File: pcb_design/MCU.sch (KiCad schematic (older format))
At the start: 14 parts, among them U1 STM32F40X_LQFP64, X2 ABM3B - 8MHz

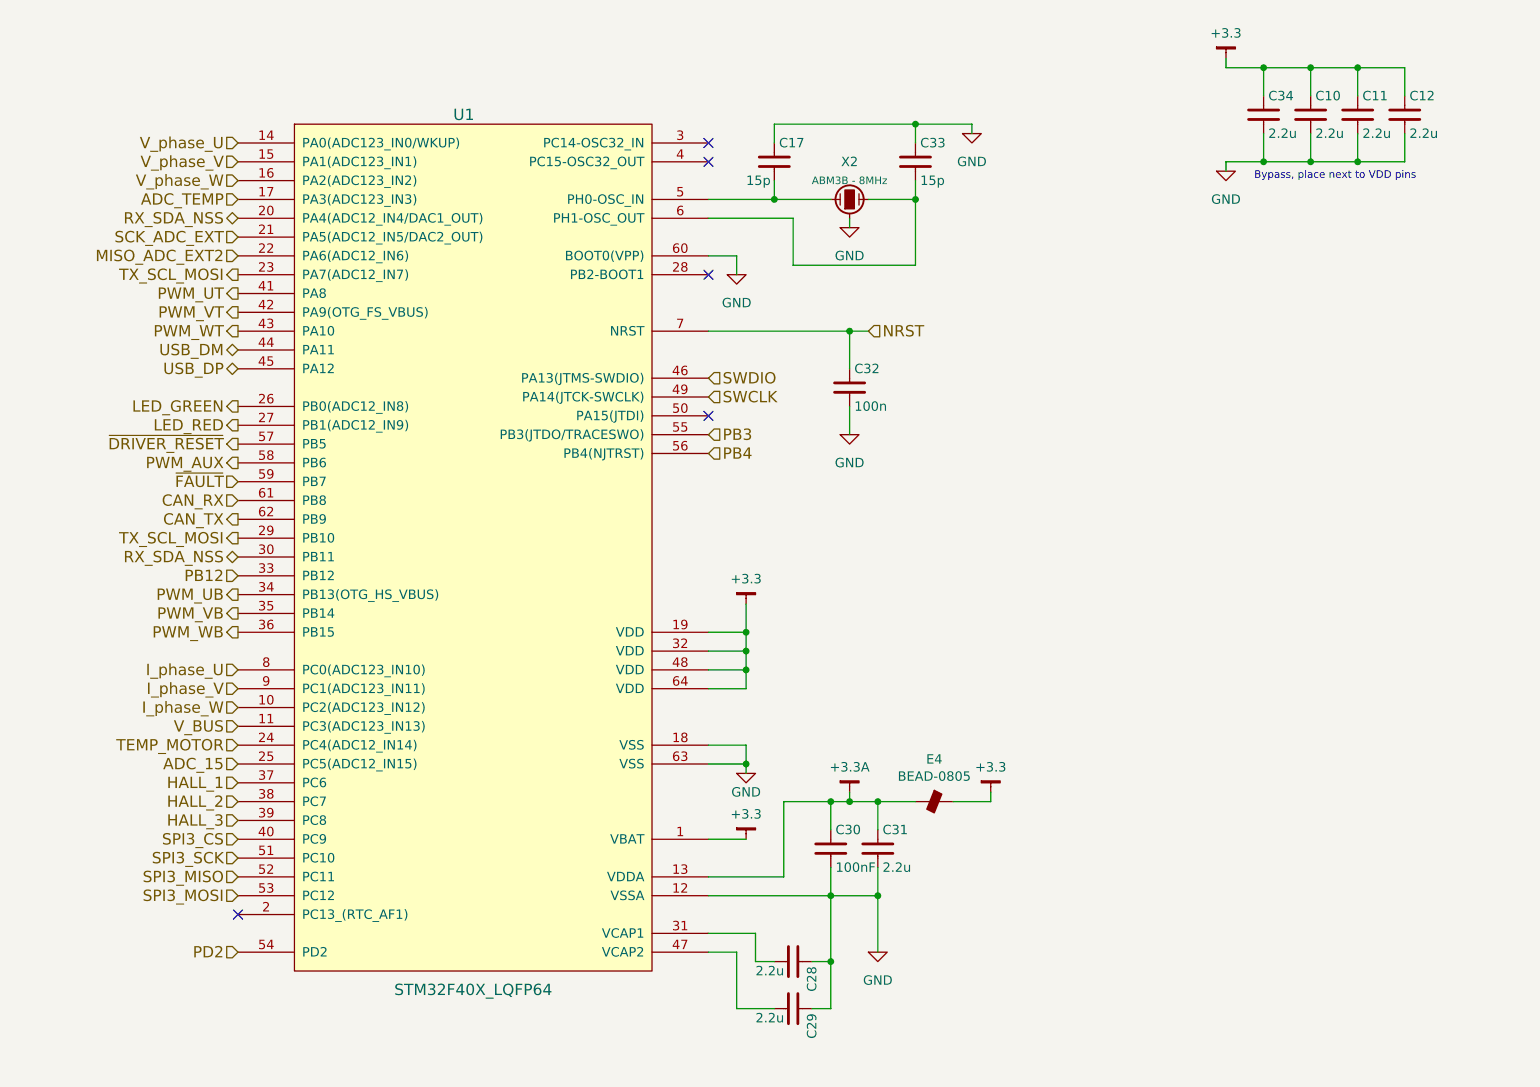
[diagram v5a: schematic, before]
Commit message: Fixed issue with non-bidirectional phase current measurement. Started routing power supplies. Changed terminal blocks from 5.00mm to 3.81mm pitch
Signed-off-by: Marcos Chaparro <mchaparro@paltatech.com>
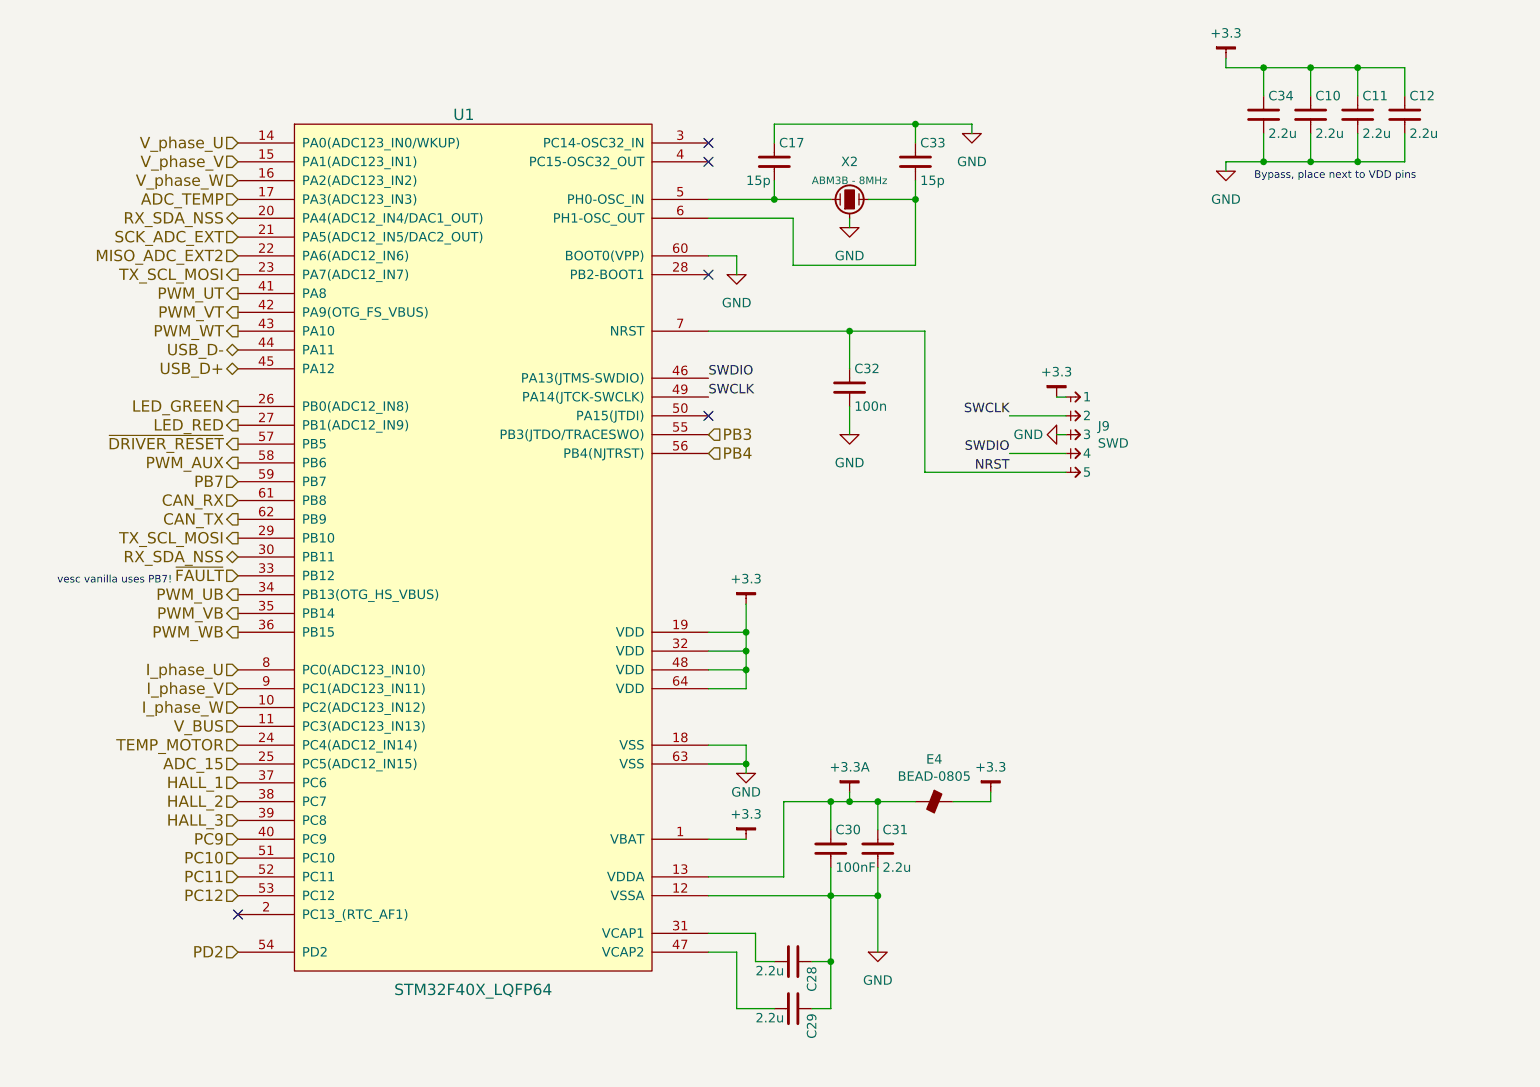
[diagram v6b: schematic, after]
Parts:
- added J9: SWD, conn-100mil:CONN-100MIL-M-1x5, symbol CONN-100MIL-M-1x5
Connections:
- net PB12 is gone; now on net ~FAULT: U1.33 (PB12)
- net +3.3: now also J9.1
- net GND: now also J9.3
- net NRST: now also J9.5
- net SWCLK: now also J9.2
- net SWDIO: now also J9.4
- net ~FAULT: no longer U1.59 (PB7)
- net SPI3_CS renamed PC9
- net SPI3_MISO renamed PC11
- net SPI3_MOSI renamed PC12
- net SPI3_SCK renamed PC10
- net USB_DM renamed USB_D-
- net USB_DP renamed USB_D+
- new net PB7: U1.59 (PB7)
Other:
- note added: "vesc vanilla uses PB7!"
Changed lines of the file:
@@
 Sheet 12 13
 Title "VESC 6.4"
-Date "2016-07-07"
-Rev "A"
-Comp "Benjamin Vedder"
+Date "2017-01-24"
+Rev "0.1"
+Comp "vedder.se + PALTA TECH S.A. + PYMCO.fr"
 Comment1 ""
 Comment2 ""
@@
 $EndDescr
 Text HLabel 3650 2600 0    60   BiDi ~ 0
-USB_DM
+USB_D-
 Text HLabel 3650 2700 0    60   BiDi ~ 0
-USB_DP
+USB_D+
 Text HLabel 3650 3200 0    60   Output ~ 0
 PWM_AUX
@@
 Text HLabel 3650 2000 0    60   Input ~ 0
 SCK_ADC_EXT
-Text HLabel 3650 3300 0    60   Input ~ 0
+Text HLabel 3650 3800 0    60   Input ~ 0
 ~FAULT
 Text HLabel 3650 2500 0    60   Output ~ 0
@@
 	8900 1650 8900 1600
 Wire Wire Line
-	6150 2500 7000 2500
+	6150 2500 7300 2500
 Wire Wire Line
 	6900 2500 6900 2700
@@
 Bypass, place next to VDD pins
 $Comp
-L GND #PWR150
+L GND #PWR0145
 U 1 1 572D84DC
 P 7550 1450
-F 0 "#PWR150" H 7550 1200 50  0001 C CNN
+F 0 "#PWR0145" H 7550 1200 50  0001 C CNN
 F 1 "GND" H 7550 1300 50  0000 C CNN
 F 2 "" H 7550 1450 60  0000 C CNN
@@
 $EndComp
 $Comp
-L GND #PWR146
+L GND #PWR0146
 U 1 1 572D84DF
 P 6900 1950
-F 0 "#PWR146" H 6900 1700 50  0001 C CNN
+F 0 "#PWR0146" H 6900 1700 50  0001 C CNN
 F 1 "GND" H 6900 1800 50  0000 C CNN
 F 2 "" H 6900 1950 60  0000 C CNN
@@
 $EndComp
 $Comp
-L GND #PWR142
+L GND #PWR0147
 U 1 1 572D84E0
 P 6300 2200
-F 0 "#PWR142" H 6300 1950 50  0001 C CNN
+F 0 "#PWR0147" H 6300 1950 50  0001 C CNN
 F 1 "GND" H 6300 2050 50  0000 C CNN
 F 2 "" H 6300 2200 60  0000 C CNN
@@
 $EndComp
 $Comp
-L GND #PWR147
+L GND #PWR0148
 U 1 1 572D84E2
 P 6900 3050
-F 0 "#PWR147" H 6900 2800 50  0001 C CNN
+F 0 "#PWR0148" H 6900 2800 50  0001 C CNN
 F 1 "GND" H 6900 2900 50  0000 C CNN
 F 2 "" H 6900 3050 60  0000 C CNN
@@
 Wire Wire Line
 	6900 3050 6900 2900
-Text HLabel 7000 2500 2    60   Input ~ 0
-NRST
-Text HLabel 6150 2750 2    60   Input ~ 0
-SWDIO
-Text HLabel 6150 2850 2    60   Input ~ 0
-SWCLK
-$Comp
-L GND #PWR149
+$Comp
+L GND #PWR0149
 U 1 1 572D84E3
 P 7050 5800
-F 0 "#PWR149" H 7050 5550 50  0001 C CNN
+F 0 "#PWR0149" H 7050 5550 50  0001 C CNN
 F 1 "GND" H 7050 5650 50  0000 C CNN
 F 2 "" H 7050 5800 60  0000 C CNN
@@
 $EndComp
 $Comp
-L GND #PWR144
+L GND #PWR0150
 U 1 1 572D84E4
 P 6350 4850
-F 0 "#PWR144" H 6350 4600 50  0001 C CNN
+F 0 "#PWR0150" H 6350 4600 50  0001 C CNN
 F 1 "GND" H 6350 4750 50  0000 C CNN
 F 2 "" H 6350 4850 60  0000 C CNN
@@
 $EndComp
 $Comp
-L GND #PWR153
+L GND #PWR0151
 U 1 1 572D84E9
 P 8900 1650
-F 0 "#PWR153" H 8900 1400 50  0001 C CNN
+F 0 "#PWR0151" H 8900 1400 50  0001 C CNN
 F 1 "GND" H 8900 1500 50  0000 C CNN
 F 2 "" H 8900 1650 60  0000 C CNN
@@
 I_phase_W
 Text HLabel 3650 5400 0    60   Input ~ 0
-SPI3_MISO
+PC11
 Text HLabel 3650 5500 0    60   Input ~ 0
-SPI3_MOSI
+PC12
 Text HLabel 3650 5300 0    60   Input ~ 0
-SPI3_SCK
+PC10
 Text HLabel 3650 5200 0    60   Input ~ 0
-SPI3_CS
+PC9
 NoConn ~ 3650 5600
 Text HLabel 3650 4800 0    60   Input ~ 0
 ADC_15
-Text HLabel 3650 3800 0    60   Input ~ 0
-PB12
+Text HLabel 3650 3300 0    60   Input ~ 0
+PB7
 Text HLabel 3650 5800 0    60   Input ~ 0
 PD2
@@
 $EndComp
 $Comp
-L +3.3 #PWR152
+L +3.3 #PWR0152
 U 1 1 588B6A3F
 P 8900 1050
-F 0 "#PWR152" H 0   100 30  0001 C CNN
+F 0 "#PWR0152" H 0   100 30  0001 C CNN
 F 1 "+3.3" H 8900 1183 50  0000 C CNN
 F 2 "" H 0   50  60  0000 C CNN
@@
 Connection ~ 6900 2500
 $Comp
-L +3.3 #PWR143
+L +3.3 #PWR0153
 U 1 1 588B6C25
 P 6350 3950
-F 0 "#PWR143" H 6400 4000 30  0001 C CNN
+F 0 "#PWR0153" H 6400 4000 30  0001 C CNN
 F 1 "+3.3" H 6350 4083 50  0000 C CNN
 F 2 "" H 0   50  60  0000 C CNN
@@
 $EndComp
 $Comp
-L +3.3 #PWR151
+L +3.3 #PWR0154
 U 1 1 588B6CC6
 P 7650 4950
-F 0 "#PWR151" H 7700 5000 30  0001 C CNN
+F 0 "#PWR0154" H 7700 5000 30  0001 C CNN
 F 1 "+3.3" H 7650 5083 50  0000 C CNN
 F 2 "" H 0   50  60  0000 C CNN
@@
 $EndComp
 $Comp
-L +3.3 #PWR145
+L +3.3 #PWR0155
 U 1 1 588B6D3A
 P 6350 5200
-F 0 "#PWR145" H 6400 5250 30  0001 C CNN
+F 0 "#PWR0155" H 6400 5250 30  0001 C CNN
 F 1 "+3.3" H 6350 5333 50  0000 C CNN
 F 2 "" H -1300 300 60  0000 C CNN
@@
 $EndComp
 $Comp
-L +3.3A #PWR148
+L +3.3A #PWR0156
 U 1 1 588B9943
 P 6900 4950
-F 0 "#PWR148" H 6950 5000 30  0001 C CNN
+F 0 "#PWR0156" H 6950 5000 30  0001 C CNN
 F 1 "+3.3A" H 6900 5083 50  0000 C CNN
 F 2 "" H -900 -500 60  0000 C CNN
@@
 	6900 4950 6900 5000
 Connection ~ 6900 5000
+$Comp
+L CONN-100MIL-M-1x5 J9
+U 1 1 5892AE40
+P 8100 2850
+F 0 "J9" H 8219 2695 50  0000 L CNN
+F 1 "SWD" H 8219 2604 50  0000 L CNN
+F 2 "conn-100mil:CONN-100MIL-M-1x5" H -450 -550 50  0001 C CNN
+F 3 "" H -450 -550 50  0000 C CNN
+	1    8100 2850
+	1    0    0    -1
+$EndComp
+$Comp
+L +3.3 #PWR0157
+U 1 1 5892B530
+P 8000 2850
+F 0 "#PWR0157" H -900 1900 30  0001 C CNN
+F 1 "+3.3" H 8000 2983 50  0000 C CNN
+F 2 "" H -900 1850 60  0000 C CNN
+F 3 "" H -900 1850 60  0000 C CNN
+	1    8000 2850
+	1    0    0    -1
+$EndComp
+Wire Wire Line
+	8000 2850 8050 2850
+Text Label 6150 2850 0    50   ~ 0
+SWCLK
+Text Label 6150 2750 0    50   ~ 0
+SWDIO
+Text Label 7750 3150 2    50   ~ 0
+SWDIO
+Wire Wire Line
+	7750 3150 8050 3150
+Wire Wire Line
+	8050 2950 7750 2950
+$Comp
+L GND #PWR0158
+U 1 1 5892B905
+P 8000 3050
+F 0 "#PWR0158" H 8000 2800 50  0001 C CNN
+F 1 "GND" V 8000 2900 50  0000 C CNN
+F 2 "" H 8000 3050 60  0000 C CNN
+F 3 "" H 8000 3050 60  0000 C CNN
+	1    8000 3050
+	0    1    1    0
+$EndComp
+Wire Wire Line
+	8000 3050 8050 3050
+Text Label 7750 2950 2    50   ~ 0
+SWCLK
+Wire Wire Line
+	8050 3250 7300 3250
+Wire Wire Line
+	7300 3250 7300 2500
+Text Label 7750 3250 2    50   ~ 0
+NRST
+Text Notes 3300 3850 2    40   ~ 0
+vesc vanilla uses PB7!
 $EndSCHEMATC

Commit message: More layout
Signed-off-by: Marcos Chaparro <mchaparro@paltatech.com>
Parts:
- added R122: 1k, IPC7351-Nominal:RESC1608X50, symbol R-0603
- added SW1: BOOTLOADER, symbol PUSH
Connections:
- net +3.3: now also SW1.2
- net GND: now also R122.2; no longer U1.60 (BOOT0(VPP))
- new net: R122.1, SW1.1, U1.60 (BOOT0(VPP))
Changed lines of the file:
@@
 	6350 3950 6350 4400
 Wire Wire Line
-	6300 2100 6300 2200
-Wire Wire Line
-	6150 2100 6300 2100
+	6450 2350 6450 2400
 Connection ~ 7250 1400
 Wire Wire Line
@@
 Bypass, place next to VDD pins
 $Comp
-L GND #PWR0145
+L GND #PWR154
 U 1 1 572D84DC
 P 7550 1450
-F 0 "#PWR0145" H 7550 1200 50  0001 C CNN
+F 0 "#PWR154" H 7550 1200 50  0001 C CNN
 F 1 "GND" H 7550 1300 50  0000 C CNN
 F 2 "" H 7550 1450 60  0000 C CNN
@@
 $EndComp
 $Comp
-L GND #PWR0146
+L GND #PWR149
 U 1 1 572D84DF
 P 6900 1950
-F 0 "#PWR0146" H 6900 1700 50  0001 C CNN
+F 0 "#PWR149" H 6900 1700 50  0001 C CNN
 F 1 "GND" H 6900 1800 50  0000 C CNN
 F 2 "" H 6900 1950 60  0000 C CNN
@@
 $EndComp
 $Comp
-L GND #PWR0147
+L GND #PWR148
 U 1 1 572D84E0
-P 6300 2200
-F 0 "#PWR0147" H 6300 1950 50  0001 C CNN
-F 1 "GND" H 6300 2050 50  0000 C CNN
-F 2 "" H 6300 2200 60  0000 C CNN
-F 3 "" H 6300 2200 60  0000 C CNN
-	1    6300 2200
+P 6450 2400
+F 0 "#PWR148" H 6450 2150 50  0001 C CNN
+F 1 "GND" H 6450 2300 50  0000 C CNN
+F 2 "" H 6450 2400 60  0000 C CNN
+F 3 "" H 6450 2400 60  0000 C CNN
+	1    6450 2400
 	1    0    0    -1
 $EndComp
@@
 $EndComp
 $Comp
-L GND #PWR0148
+L GND #PWR150
 U 1 1 572D84E2
 P 6900 3050
-F 0 "#PWR0148" H 6900 2800 50  0001 C CNN
+F 0 "#PWR150" H 6900 2800 50  0001 C CNN
 F 1 "GND" H 6900 2900 50  0000 C CNN
 F 2 "" H 6900 3050 60  0000 C CNN
@@
 	6900 3050 6900 2900
 $Comp
-L GND #PWR0149
+L GND #PWR152
 U 1 1 572D84E3
 P 7050 5800
-F 0 "#PWR0149" H 7050 5550 50  0001 C CNN
+F 0 "#PWR152" H 7050 5550 50  0001 C CNN
 F 1 "GND" H 7050 5650 50  0000 C CNN
 F 2 "" H 7050 5800 60  0000 C CNN
@@
 $EndComp
 $Comp
-L GND #PWR0150
+L GND #PWR146
 U 1 1 572D84E4
 P 6350 4850
-F 0 "#PWR0150" H 6350 4600 50  0001 C CNN
+F 0 "#PWR146" H 6350 4600 50  0001 C CNN
 F 1 "GND" H 6350 4750 50  0000 C CNN
 F 2 "" H 6350 4850 60  0000 C CNN
@@
 $EndComp
 $Comp
-L GND #PWR0151
+L GND #PWR159
 U 1 1 572D84E9
 P 8900 1650
-F 0 "#PWR0151" H 8900 1400 50  0001 C CNN
+F 0 "#PWR159" H 8900 1400 50  0001 C CNN
 F 1 "GND" H 8900 1500 50  0000 C CNN
 F 2 "" H 8900 1650 60  0000 C CNN
@@
 $EndComp
 $Comp
-L +3.3 #PWR0152
+L +3.3 #PWR158
 U 1 1 588B6A3F
 P 8900 1050
-F 0 "#PWR0152" H 0   100 30  0001 C CNN
+F 0 "#PWR158" H 0   100 30  0001 C CNN
 F 1 "+3.3" H 8900 1183 50  0000 C CNN
 F 2 "" H 0   50  60  0000 C CNN
@@
 Connection ~ 6900 2500
 $Comp
-L +3.3 #PWR0153
+L +3.3 #PWR145
 U 1 1 588B6C25
 P 6350 3950
-F 0 "#PWR0153" H 6400 4000 30  0001 C CNN
+F 0 "#PWR145" H 6400 4000 30  0001 C CNN
 F 1 "+3.3" H 6350 4083 50  0000 C CNN
 F 2 "" H 0   50  60  0000 C CNN
@@
 $EndComp
 $Comp
-L +3.3 #PWR0154
+L +3.3 #PWR155
 U 1 1 588B6CC6
 P 7650 4950
-F 0 "#PWR0154" H 7700 5000 30  0001 C CNN
+F 0 "#PWR155" H 7700 5000 30  0001 C CNN
 F 1 "+3.3" H 7650 5083 50  0000 C CNN
 F 2 "" H 0   50  60  0000 C CNN
@@
 $EndComp
 $Comp
-L +3.3 #PWR0155
+L +3.3 #PWR147
 U 1 1 588B6D3A
 P 6350 5200
-F 0 "#PWR0155" H 6400 5250 30  0001 C CNN
+F 0 "#PWR147" H 6400 5250 30  0001 C CNN
 F 1 "+3.3" H 6350 5333 50  0000 C CNN
 F 2 "" H -1300 300 60  0000 C CNN
@@
 $EndComp
 $Comp
-L +3.3A #PWR0156
+L +3.3A #PWR151
 U 1 1 588B9943
 P 6900 4950
-F 0 "#PWR0156" H 6950 5000 30  0001 C CNN
+F 0 "#PWR151" H 6950 5000 30  0001 C CNN
 F 1 "+3.3A" H 6900 5083 50  0000 C CNN
 F 2 "" H -900 -500 60  0000 C CNN
@@
 $EndComp
 $Comp
-L +3.3 #PWR0157
+L +3.3 #PWR156
 U 1 1 5892B530
 P 8000 2850
-F 0 "#PWR0157" H -900 1900 30  0001 C CNN
+F 0 "#PWR156" H -900 1900 30  0001 C CNN
 F 1 "+3.3" H 8000 2983 50  0000 C CNN
 F 2 "" H -900 1850 60  0000 C CNN
@@
 	8050 2950 7750 2950
 $Comp
-L GND #PWR0158
+L GND #PWR157
 U 1 1 5892B905
 P 8000 3050
-F 0 "#PWR0158" H 8000 2800 50  0001 C CNN
+F 0 "#PWR157" H 8000 2800 50  0001 C CNN
 F 1 "GND" V 8000 2900 50  0000 C CNN
 F 2 "" H 8000 3050 60  0000 C CNN
@@
 Text Notes 3300 3850 2    40   ~ 0
 vesc vanilla uses PB7!
+$Comp
+L R-0603 R122
+U 1 1 588E0131
+P 6450 2250
+F 0 "R122" H 6512 2296 50  0000 L CNN
+F 1 "1k" H 6512 2205 50  0000 L CNN
+F 2 "IPC7351-Nominal:RESC1608X50" H 50  50  50  0001 C CNN
+F 3 "" H 50  100 60  0000 C CNN
+F 4 "RES SMD 1k 5% [0603]" H 800 600 60  0001 C CNN "BOM"
+	1    6450 2250
+	-1   0    0    -1
+$EndComp
+Wire Wire Line
+	6150 2100 6550 2100
+Wire Wire Line
+	6450 2100 6450 2150
+$Comp
+L PUSH SW1
+U 1 1 588E02FB
+P 6900 2350
+F 0 "SW1" H 6750 2400 50  0000 C CNN
+F 1 "BOOTLOADER" H 6900 2300 40  0000 C CNN
+F 2 "" H -250 0   60  0000 C CNN
+F 3 "" H -250 0   60  0000 C CNN
+	1    6900 2350
+	1    0    0    -1
+$EndComp
+Wire Wire Line
+	6550 2100 6550 2350
+Wire Wire Line
+	6550 2350 6750 2350
+Connection ~ 6450 2100
+$Comp
+L +3.3 #PWR153
+U 1 1 588E04AA
+P 7150 2350
+F 0 "#PWR153" H -1750 1400 30  0001 C CNN
+F 1 "+3.3" H 7150 2450 50  0000 C CNN
+F 2 "" H -1750 1350 60  0000 C CNN
+F 3 "" H -1750 1350 60  0000 C CNN
+	1    7150 2350
+	1    0    0    -1
+$EndComp
+Wire Wire Line
+	7150 2350 7050 2350
 $EndSCHEMATC
